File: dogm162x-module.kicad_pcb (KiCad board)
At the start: 2 copper layers, 99.1 x 53.9 mm, 6 parts, among them P1 CONN_01X06

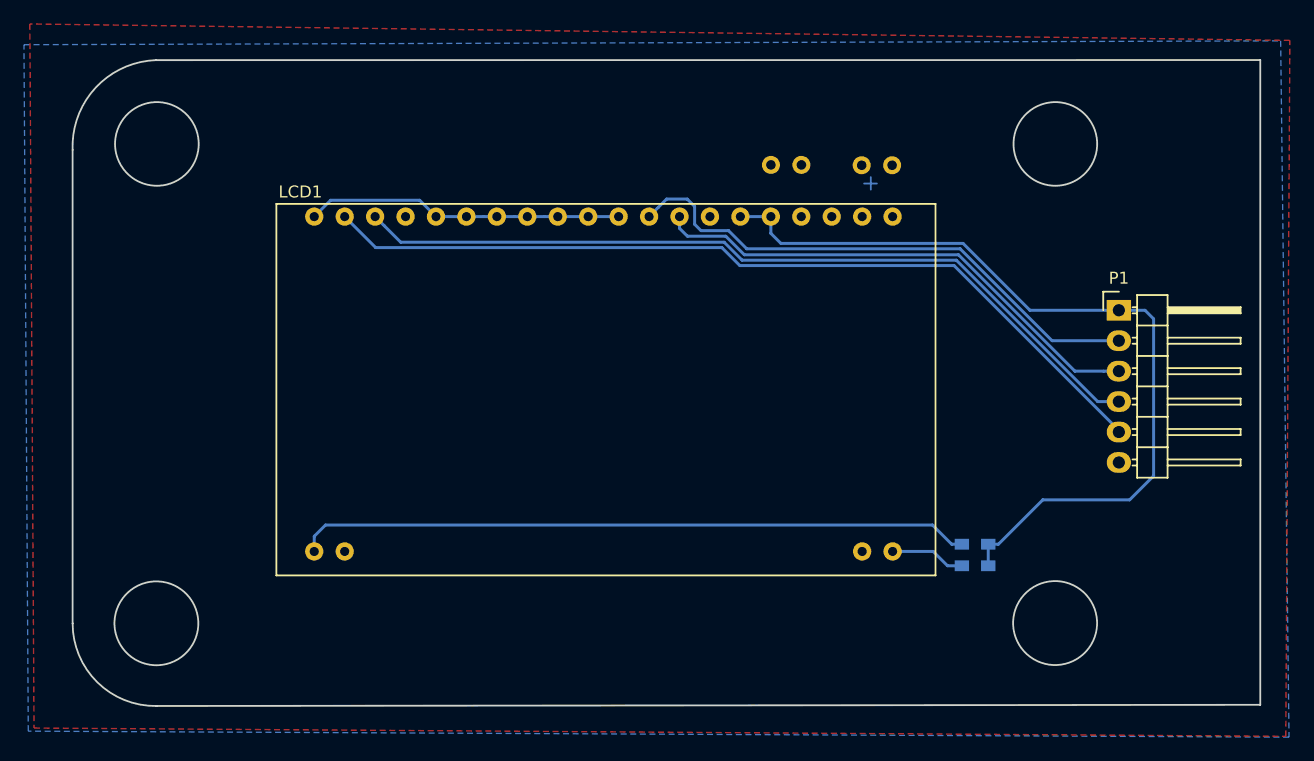
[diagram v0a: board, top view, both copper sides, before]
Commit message: redesigned board
added new outlines
switched capacitors to smd types
corrected position of the 3d display model
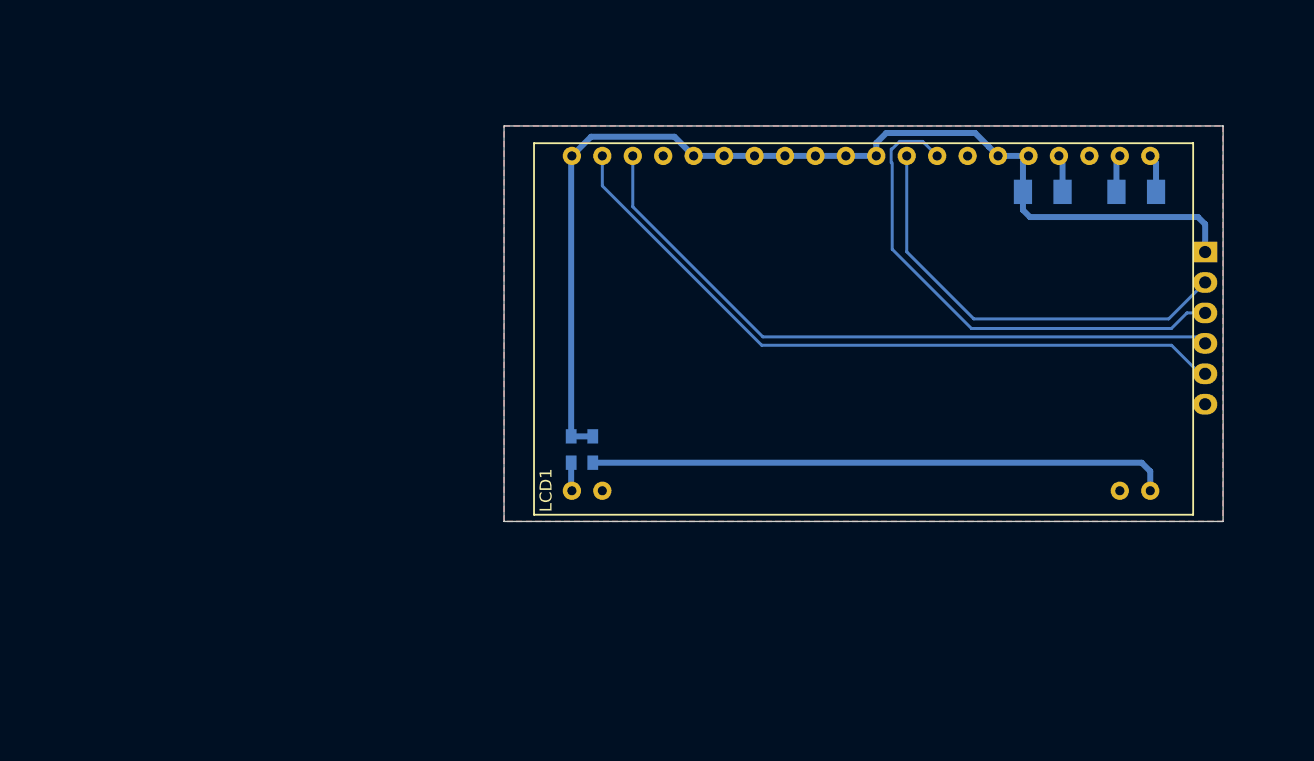
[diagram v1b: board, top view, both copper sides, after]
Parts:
- removed R11: 15R, Resistors_SMD:R_0603_HandSoldering
- added R2: 15R, Resistors_SMD:R_0603_HandSoldering, B.Cu at (147.4, 110.0)
- C1: footprint Capacitors_Elko_ThroughHole:Elko_vert_11.2x6.3mm_RM2.5_CopperClear -> SMD_Packages:SMD-1206_Pol
- C2: footprint Capacitors_Elko_ThroughHole:Elko_vert_11x5mm_RM2.5 -> SMD_Packages:SMD-1206_Pol
- P1: moved to B.Cu
- moved R1 34.6 mm to (145.6, 110.0), turned to 270 degrees
- moved C2 23.0 mm to (192.8, 88.5)
- moved LCD1 22.1 mm to (170.0, 99.9)
- moved C1 20.3 mm to (184.9, 88.5)
- moved P1 8.69 mm to (198.5, 93.5), turned to 180 degrees
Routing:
- net /A1: track 56.4 -> 2.36 mm
- net /A2: track 6.28 -> 48.5 mm
- net /RS: track 72.1 -> 59.3 mm
- net /CS: track 68.5 -> 56.7 mm
- net /CLK: track 45.6 -> 36.5 mm
- net VCC: track 96.4 -> 89.6 mm
- net /CAP1N: track 0.00 -> 3.20 mm
- net /VOUT: track 0.00 -> 3.12 mm
- net /CAP1P: track 0.00 -> 3.12 mm
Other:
- board size 99.1 x 53.9 mm -> 60 x 33 mm

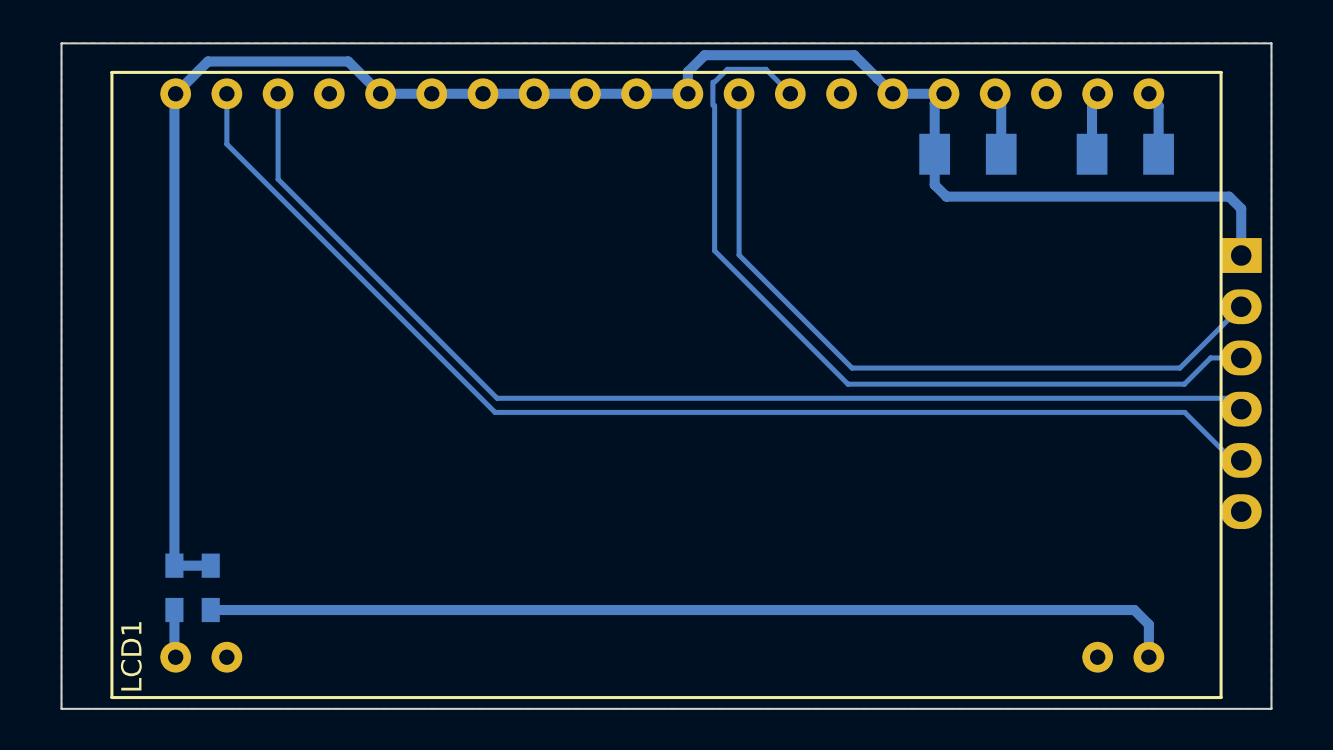
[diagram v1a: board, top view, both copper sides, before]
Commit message: beautification and minor changes
resized board outlines
changed 6 pin header to 8 pin header to get an extra pin for backlight
power
added silkscreen text
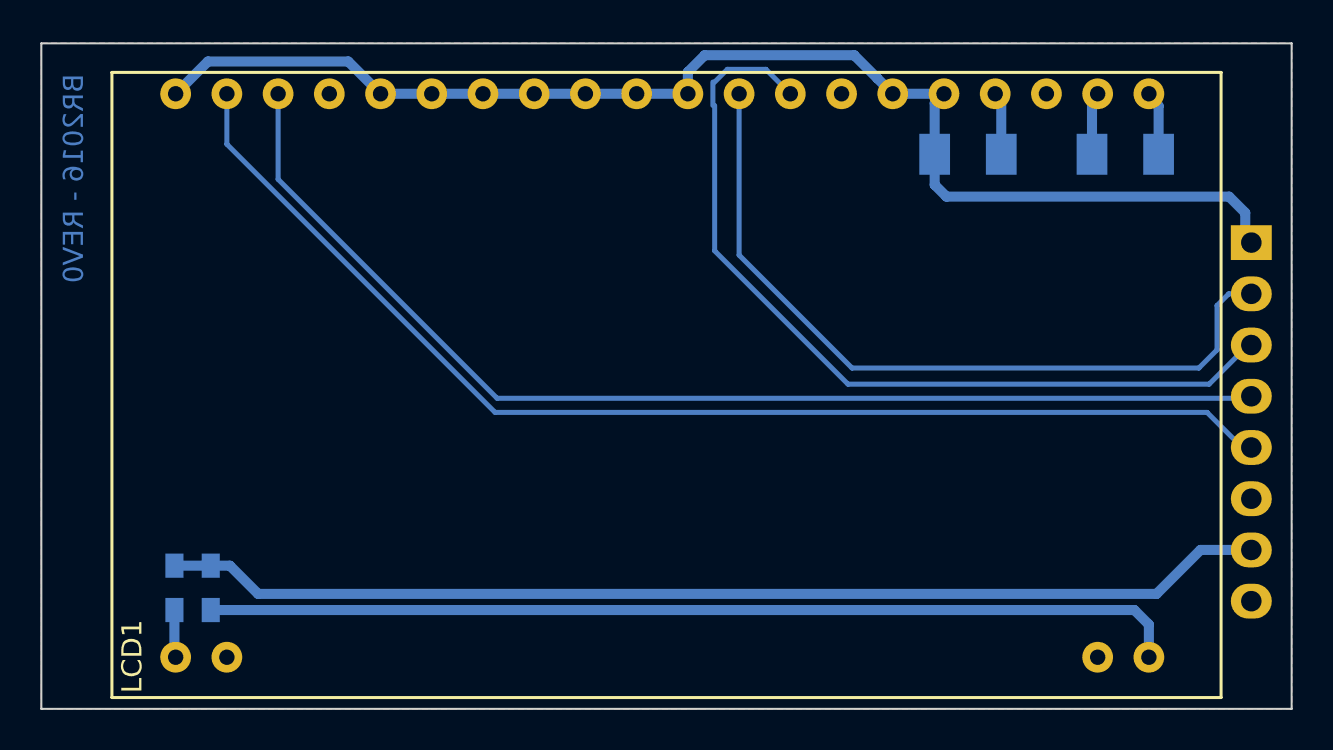
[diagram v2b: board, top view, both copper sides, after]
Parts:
- P1: value CONN_01X06 -> CONN_01X08; footprint Pin_Headers:Pin_Header_Angled_1x06 -> Socket_Strips:Socket_Strip_Straight_1x08
- moved P1 0.81 mm to (199.0, 92.9), turned to 270 degrees
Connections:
- R1 pad 1: VCC -> /VCC_BACKLIGHT
- R2 pad 1: VCC -> /VCC_BACKLIGHT
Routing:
- net /VCC_BACKLIGHT: track 0.00 -> 54.6 mm
- net VCC: track 89.6 -> 63.9 mm
- net /CLK: track 36.5 -> 38.2 mm
- net /SI: track 42.3 -> 43.2 mm
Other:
- board size 60 x 33 mm -> 62 x 33 mm
- board text added: "BR2016 - REV0"
- board text added: "DOG-M162X Display Module"
